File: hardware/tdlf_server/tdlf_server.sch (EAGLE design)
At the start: 34 parts, among them IC4 DAC8564, IC6 OPA4171

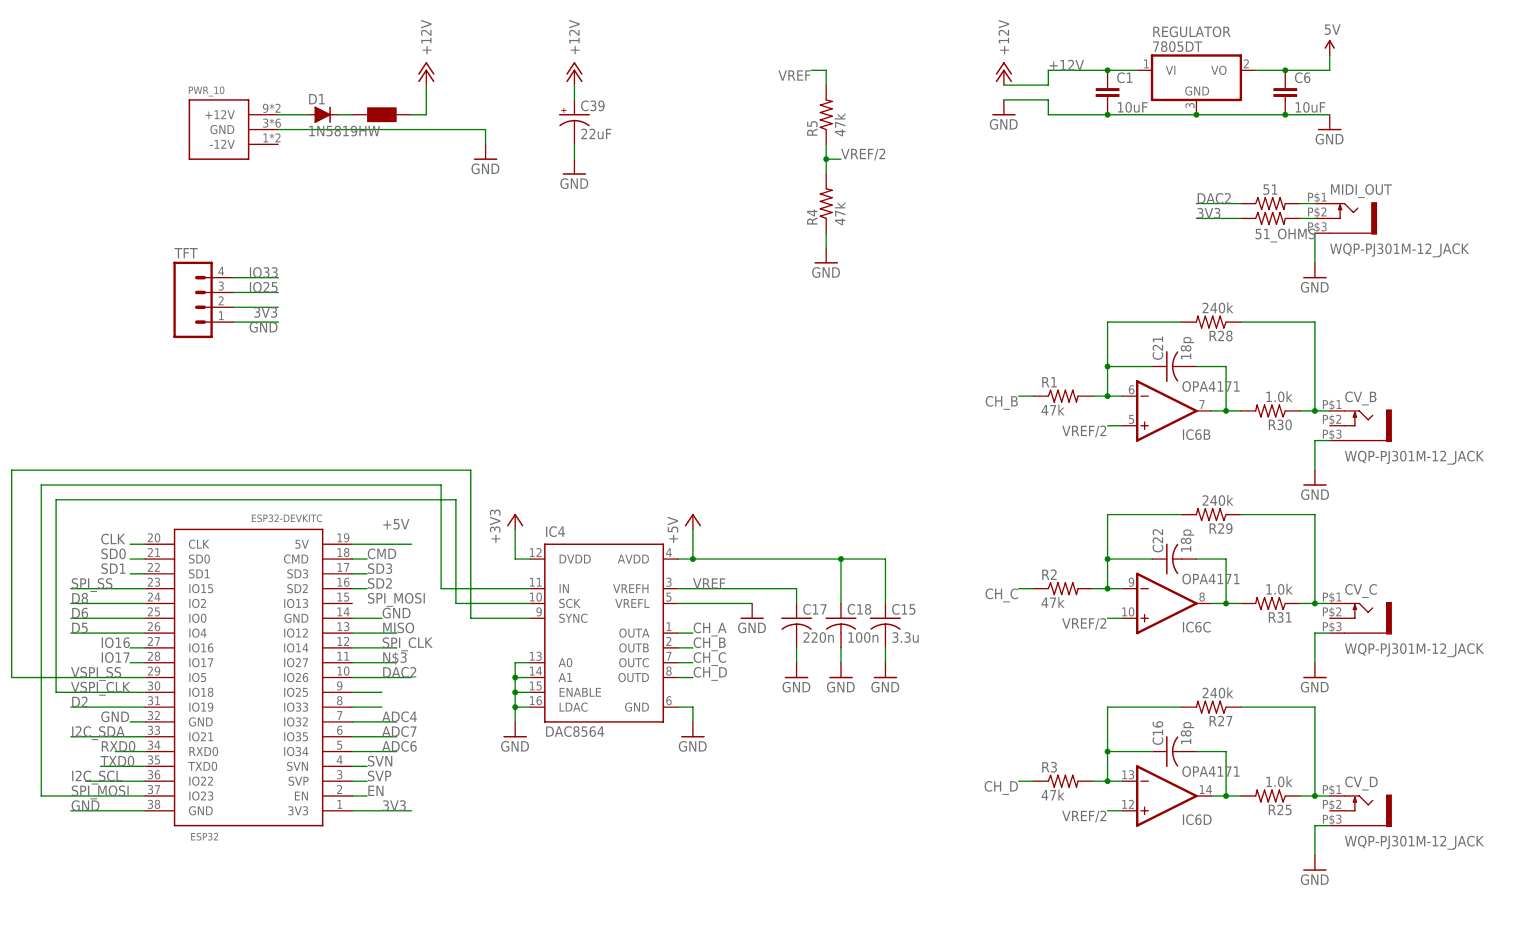
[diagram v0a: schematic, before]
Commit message: Moving to TRS for midi and three CV outputs
For future use with physical interfaces sending sensor data via UDP to the server.
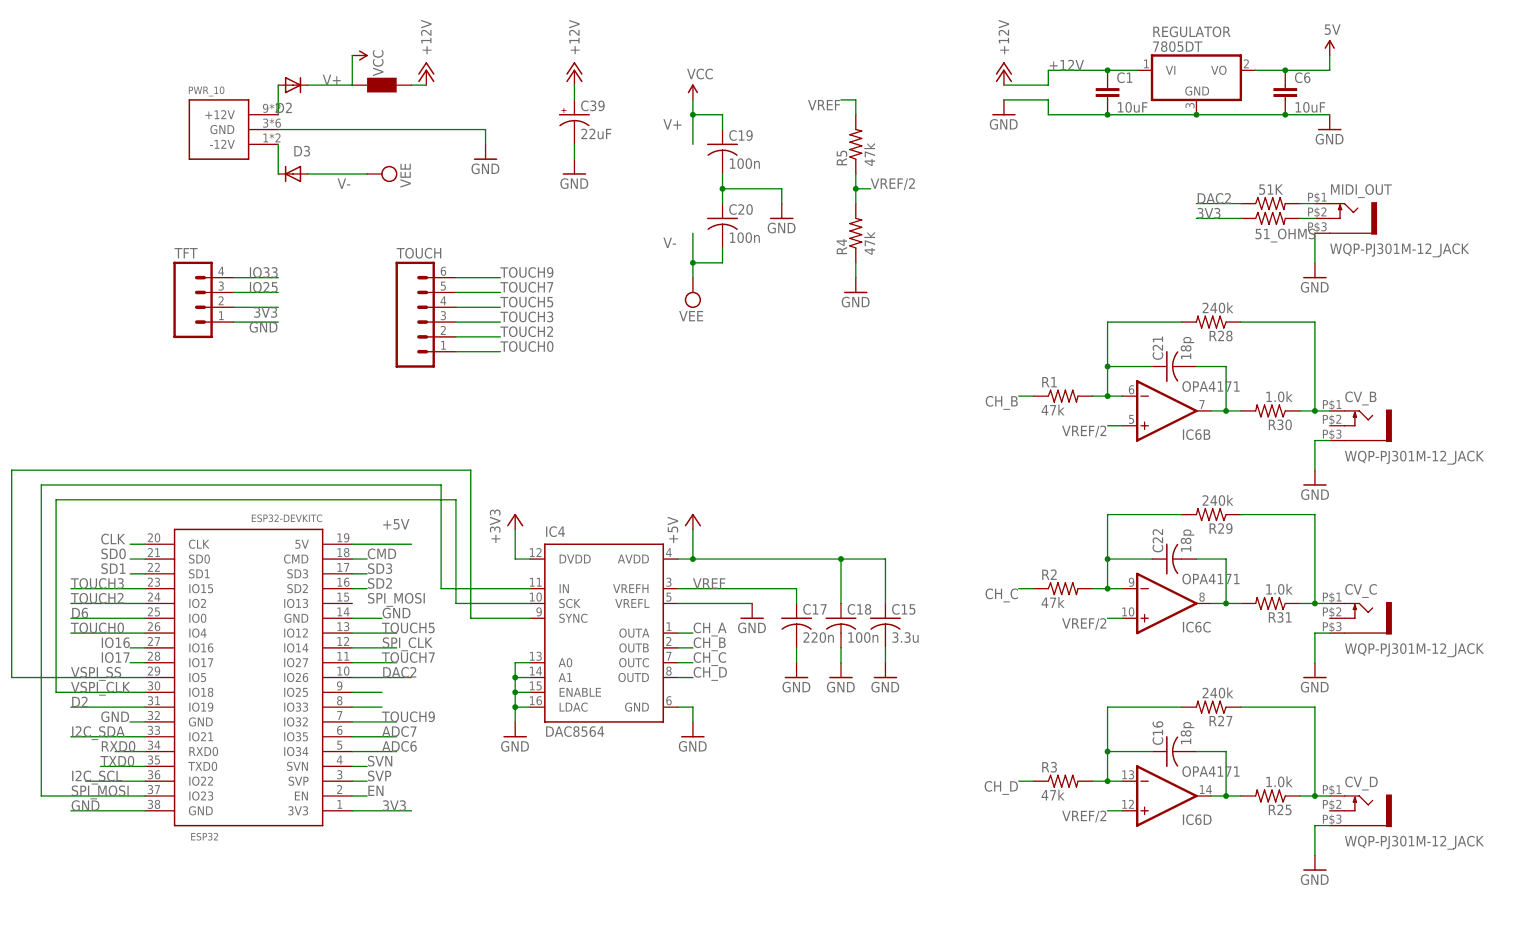
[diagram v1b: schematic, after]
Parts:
- removed D1: 1N5819HW, parts_aman:DIODE
- added C19, C20: 100n, rcl:C-USC0603
- added D2: B0450, diode:DIODE-SOD123
- added D3: B0540, diode:DIODE-SOD123
- added TOUCH: (no value), SparkFun-Connectors:M06LOCK_LONGPADS
- renumbered 51 to 51K
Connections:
- removed net +12: D1.+, PWR_10.+12V
- removed net ADC4: ESP32.IO32
- removed net D5: ESP32.IO4
- removed net D8: ESP32.IO2
- removed net MISO: ESP32.IO12
- removed net N$3: ESP32.IO27
- removed net N$47: D1.-, F1.P$2
- removed net SPI_SS: ESP32.IO15
- new net N$1: D3.C, PWR_10.-12V
- new net N$4: D2.A, PWR_10.+12V
- new net TOUCH0: ESP32.IO4, TOUCH.1
- new net TOUCH2: ESP32.IO2, TOUCH.2
- new net TOUCH3: ESP32.IO15, TOUCH.3
- new net TOUCH5: ESP32.IO12, TOUCH.4
- new net TOUCH7: ESP32.IO27, TOUCH.5
- new net TOUCH9: ESP32.IO32, TOUCH.6
- new net V+: C19.1, D2.C, F1.P$2
- new net V-: C20.2, D3.A
- net GND: now also C19.2, C20.1
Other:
- moved on the sheet: R4, R5

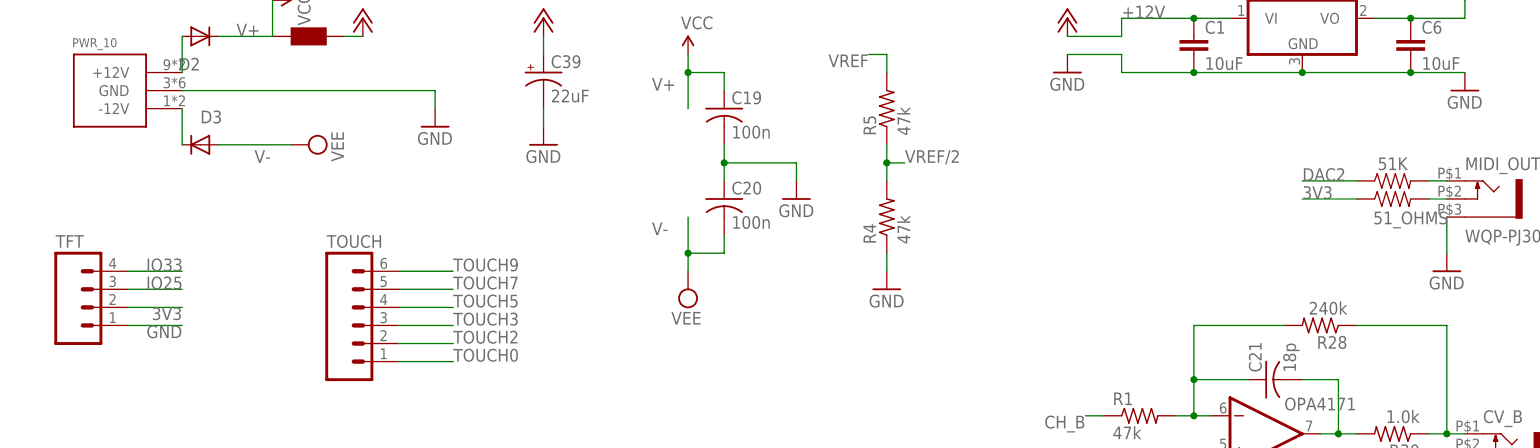
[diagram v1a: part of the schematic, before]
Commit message: Now with 3 CV outputs !
Midi TRS out works
CV out : the hardware works but the code needs to be implemented. Help needed :).
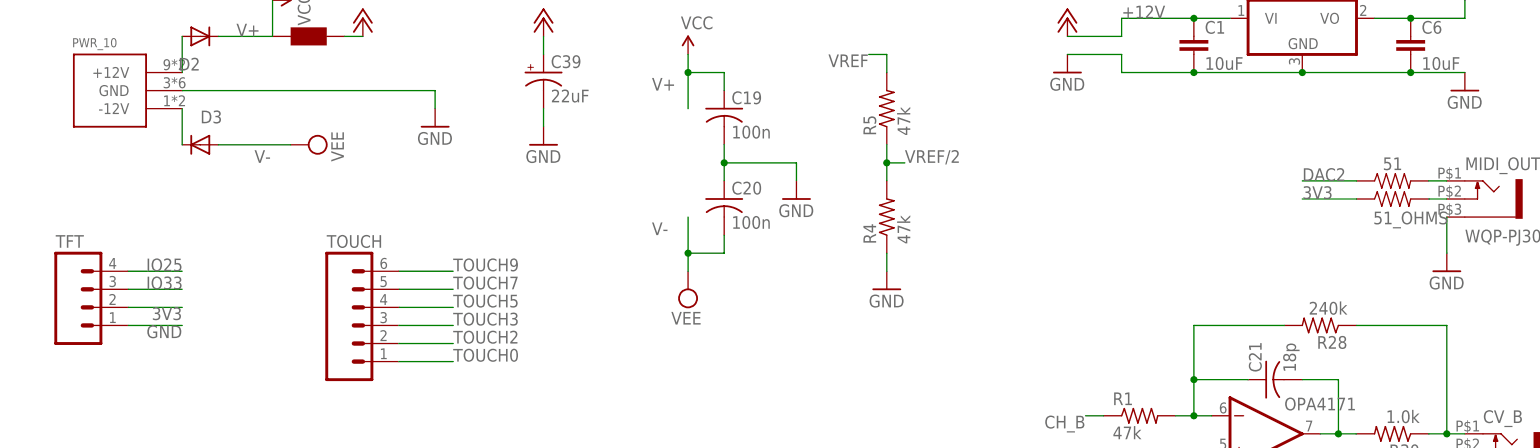
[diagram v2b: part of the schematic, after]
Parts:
- renumbered 51K to 51
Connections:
- net IO25: now also TFT.4; no longer TFT.3
- net IO33: now also TFT.3; no longer TFT.4
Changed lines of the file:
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@@
 <part name="TFT" library="SparkFun-Connectors" library_urn="urn:adsk.eagle:library:6242394" deviceset="M04" device="PTH" package3d_urn="urn:adsk.eagle:package:6242978/1"/>
 <part name="51_OHMS" library="SparkFun-Resistors" library_urn="urn:adsk.eagle:library:532" deviceset="RESISTOR" device="1206" package3d_urn="urn:adsk.eagle:package:39654/1" value=" "/>
-<part name="51K" library="SparkFun-Resistors" library_urn="urn:adsk.eagle:library:532" deviceset="RESISTOR" device="1206" package3d_urn="urn:adsk.eagle:package:39654/1" value=" "/>
+<part name="51" library="SparkFun-Resistors" library_urn="urn:adsk.eagle:library:532" deviceset="RESISTOR" device="1206" package3d_urn="urn:adsk.eagle:package:39654/1" value=" "/>
 <part name="PWR_10" library="parts_aman" deviceset="POWER_SIMPLE" device="10"/>
 <part name="F1" library="parts_aman" deviceset="FERRITE-BEAD" device="0805" value="Würth Electronics 742792664"/>
@@
 <attribute name="VALUE" x="213.36" y="115.316" size="1.778" layer="96" font="vector" align="top-center"/>
 </instance>
-<instance part="51K" gate="G$1" x="213.36" y="119.38" smashed="yes">
+<instance part="51" gate="G$1" x="213.36" y="119.38" smashed="yes">
 <attribute name="NAME" x="213.36" y="120.904" size="1.778" layer="95" font="vector" align="bottom-center"/>
 <attribute name="VALUE" x="213.36" y="115.316" size="1.778" layer="96" font="vector" align="top-center"/>
@@
 <net name="PIN27" class="0">
 <segment>
-<pinref part="51K" gate="G$1" pin="2"/>
+<pinref part="51" gate="G$1" pin="2"/>
 <pinref part="MIDI_OUT" gate="G$1" pin="2"/>
 <wire x1="218.44" y1="119.38" x2="220.98" y2="119.38" width="0.1524" layer="91"/>
@@
 </segment>
 <segment>
-<pinref part="TFT" gate="G$1" pin="4"/>
-<wire x1="35.56" y1="106.68" x2="43.18" y2="106.68" width="0.1524" layer="91"/>
-<label x="38.1" y="106.68" size="1.778" layer="95"/>
+<label x="38.1" y="104.14" size="1.778" layer="95"/>
+<pinref part="TFT" gate="G$1" pin="3"/>
+<wire x1="43.18" y1="104.14" x2="35.56" y2="104.14" width="0.1524" layer="91"/>
 </segment>
 </net>
@@
 </segment>
 <segment>
-<pinref part="TFT" gate="G$1" pin="3"/>
-<wire x1="35.56" y1="104.14" x2="43.18" y2="104.14" width="0.1524" layer="91"/>
-<label x="38.1" y="104.14" size="1.778" layer="95"/>
+<label x="38.1" y="106.68" size="1.778" layer="95"/>
+<wire x1="43.18" y1="106.68" x2="35.56" y2="106.68" width="0.1524" layer="91"/>
+<pinref part="TFT" gate="G$1" pin="4"/>
 </segment>
 </net>
@@
 </segment>
 <segment>
-<pinref part="51K" gate="G$1" pin="1"/>
+<pinref part="51" gate="G$1" pin="1"/>
 <wire x1="208.28" y1="119.38" x2="200.66" y2="119.38" width="0.1524" layer="91"/>
 <label x="200.66" y="119.38" size="1.778" layer="95"/>

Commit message: Version 0.5 ready for CV outputs
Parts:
- removed C15: 3.3u, rcl:C-USC0603
- removed C17: 220n, rcl:C-USC0603
- removed C18: 100n, rcl:C-USC0603
- removed IC4: DAC8564, og-dac:DAC8564
- removed R4, R5: 47k, rcl:R-US_R1206
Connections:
- removed net +3V3: IC4.DVDD
- removed net CH_A: IC4.OUTA
- removed net CH_B: IC4.OUTB, R1.1
- removed net CH_C: IC4.OUTC, R2.1
- removed net CH_D: IC4.OUTD, R3.1
- removed net N$55: CV_C.2, R29.1, R31.1
- removed net N$58: CV_D.2, R25.1, R27.1
- removed net SPI_MOSI: ESP32.IO23, IC4.IN
- removed net VREF: C17.1, IC4.VREFH, R5.2
- removed net VREF/2: IC6B.+IN, IC6C.+IN, IC6D.+IN, R4.2, R5.1
- removed net VSPI_CLK: ESP32.IO18, IC4.SCK
- removed net VSPI_SS: ESP32.IO5, IC4.SYNC
- new net DAC_B: ESP32.IO5, IC6B.+IN
- new net DAC_C: ESP32.IO23, IC6C.+IN
- new net DAC_D: ESP32.IO18, IC6D.+IN
- new net N$3: CV_C.2, R31.1
- new net N$5: CV_D.2, R25.1
- net +5V: no longer C15.1, C18.1, IC4.AVDD
- net GND: now also R1.1, R2.1, R3.1; no longer C15.2, C17.2, C18.2, IC4.A0, IC4.A1, IC4.ENABLE, IC4.GND, IC4.LDAC, IC4.VREFL, R4.1
- net N$50: now also R28.1
- net N$51: now also R29.1
- net N$52: now also R27.1
- net N$63: no longer R28.1
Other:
- moved on the sheet: C16, C21, C22, CV_B, CV_C, CV_D, IC6B, IC6C, IC6D, R1, R2, R25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
